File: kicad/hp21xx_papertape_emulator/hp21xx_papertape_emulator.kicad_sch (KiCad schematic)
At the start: 154 parts, among them J1 SWD, J2 SERIAL, J3 Micro_SD_Card_Det_Hirose_DM3AT, J5 Conn_02x13_Odd_Even, Q1 2N7002, Q10 2N7002, Q11 2N7002, Q12 BSS84, Q13 2N7002, Q14 2N7002, Q15 BSS84, Q2 2N7002, Q3 2N7002, Q4 2N7002, Q5 2N7002, Q6 2N7002, Q7 2N7002, Q8 2N7002, Q9 2N7002, SW1 Select, SW2 Up, SW3 Down, U1 TLV75533PDRV, U2 STM32F103C8Tx, U3 USBLC6-2SC6, U4 AP3012, U6 74LVC14, U7 74LVC245, Y1 8MHz

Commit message: Fixed issues.
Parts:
- removed R84, R90: 100, Resistor_SMD:R_0402_1005Metric, symbol Device:R_Small
- added C12, C13: 4.7u, Capacitor_SMD:C_1206_3216Metric, symbol Device:C_Small
- added R47, R48: 100, Resistor_SMD:R_0402_1005Metric, symbol Device:R_Small
- J5: now left out of the parts list
- Q1, Q10, Q11, Q13, Q14, Q2, Q3, Q4, Q5, Q6, Q7, Q8, Q9: value 2N7002 -> BSS138; LCSC C22446827 -> C53113928
- Q12, Q15: value BSS84 -> PMOS; LCSC C82079 -> (none)
- R104, R45, R56, R59, R62, R65, R68, R71, R74, R77, R80, R83: LCSC C25531 -> C25744
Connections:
- net GND: now also C12.2, C13.2
- net PU12V: now also C12.1
- net PU5V: now also C13.1
- net at Q15.2 (G): now also R48.2
- net at Q12.2 (G): now also R47.2
- net at Q14.1 (D), R89.2: now also R48.1
- net at Q13.1 (D), R85.2, R88.1: now also R47.1

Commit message: Fixed problems with net unconnected.
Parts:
- added R49, R50: 10k, Resistor_SMD:R_0402_1005Metric, symbol Device:R_Small
- Q12, Q15: value PMOS -> BSS84; LCSC (none) -> C41354933
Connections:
- net +12V: now also R50.1
- net +5V: now also R49.1
- net at Q15.2 (G), R48.2: now also R49.2
- net at Q12.2 (G), R47.2: now also R50.2

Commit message: spin 2
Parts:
- added D10, D11, D12, D13, D14, D15, D16, D17, D18, D19, D20, D21, D22, D23, D24, D25, D26, D27, D28, D29, D8, D9: BAT54J, Diode_SMD:D_SOD-523, symbol Diode:BAT54J
- added R51, R52: 10k, Resistor_SMD:R_0402_1005Metric, symbol Device:R_Small
- H2, H4, H6, H8: footprint MountingHole:MountingHole_2.2mm_M2 -> MountingHole:MountingHole_2.5mm
- L1: footprint Inductor_SMD:L_0805_2012Metric -> Inductor_SMD:L_Sunlord_SWPA3010S; LCSC C88172 -> C2049730
- Q1, Q10, Q11, Q13, Q14, Q2, Q3, Q4, Q5, Q6, Q7, Q8, Q9: symbol Simulation_SPICE:NMOS -> Transistor_FET:Q_NMOS_GSD
- Q12, Q15: symbol Simulation_SPICE:PMOS -> Transistor_FET:Q_PMOS_GSD
- R1, R2: value 2k -> 10k; LCSC C4109 -> C25744
- R11, R13, R15, R17, R24, R27, R33, R35, R37, R41: footprint Resistor_SMD:R_0402_1005Metric -> Resistor_SMD:R_0805_2012Metric; LCSC C25104 -> C17630
- R87: value 100k -> 1k; LCSC C25741 -> C11702
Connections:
- net +12V: now also Q12.2 (S); no longer Q12.1 (D)
- net +5V: now also Q15.2 (S); no longer Q15.1 (D)
- net GND: now also J3.9 (DET_B), Q1.2 (S), Q10.2 (S), Q11.2 (S), Q13.2 (S), Q14.2 (S), Q2.2 (S), Q3.2 (S), Q4.2 (S), Q5.2 (S), Q6.2 (S), Q7.2 (S), Q8.2 (S), Q9.2 (S), R51.2, R52.2; no longer Q1.3 (S), Q10.3 (S), Q11.3 (S), Q13.3 (S), Q14.3 (S), Q2.3 (S), Q3.3 (S), Q4.3 (S), Q5.3 (S), Q6.3 (S), Q7.3 (S), Q8.3 (S), Q9.3 (S)
- net OUT0: now also Q2.3 (D); no longer Q2.1 (D)
- net OUT1: now also Q3.3 (D); no longer Q3.1 (D)
- net OUT2: now also Q6.3 (D); no longer Q6.1 (D)
- net OUT3: now also Q7.3 (D); no longer Q7.1 (D)
- net OUT4: now also Q8.3 (D); no longer Q8.1 (D)
- net OUT5: now also Q9.3 (D); no longer Q9.1 (D)
- net OUT6: now also Q10.3 (D); no longer Q10.1 (D)
- net OUT7: now also Q11.3 (D); no longer Q11.1 (D)
- net OUTFP: now also Q1.3 (D); no longer Q1.1 (D)
- net OUTFR: now also Q4.3 (D); no longer Q4.1 (D)
- net PAPER_LOW: now also Q5.3 (D); no longer Q5.1 (D)
- net PU12V: now also D11.2 (A), D13.2 (A), D15.2 (A), D17.2 (A), D18.2 (A), D21.2 (A), D23.2 (A), D25.2 (A), D26.2 (A), D28.2 (A), D9.2 (A), R52.1; no longer R45.1, R56.1, R59.1, R62.1, R65.1, R68.1, R71.1, R74.1, R77.1, R80.1, R83.1
- net PU5V: now also D10.2 (A), D12.2 (A), D14.2 (A), D16.2 (A), D19.2 (A), D20.2 (A), D22.2 (A), D24.2 (A), D27.2 (A), D29.2 (A), D8.2 (A), R51.1; no longer R100.1, R101.1, R102.1, R103.1, R46.1, R94.1, R95.1, R96.1, R97.1, R98.1, R99.1
- net at R72.2, R73.1: now also Q8.1 (G); no longer Q8.2 (G)
- net at R48.1, R89.2: now also Q14.3 (D); no longer Q14.1 (D)
- net at R48.2, R49.2: now also Q15.1 (G); no longer Q15.2 (G)
- net at R10.2, R19.1: now also Q7.1 (G); no longer Q7.2 (G)
- net at R78.2, R79.1: now also Q10.1 (G); no longer Q10.2 (G)
- net at R86.2, R87.1: now also Q13.1 (G); no longer Q13.2 (G)
- net at R47.1, R85.2, R88.1: now also Q13.3 (D); no longer Q13.1 (D)
- net at R47.2, R50.2: now also Q12.1 (G); no longer Q12.2 (G)
- net at R63.2, R64.1: now also Q4.1 (G); no longer Q4.2 (G)
- net at R88.2, R93.1: now also Q14.1 (G); no longer Q14.2 (G)
- net at R75.2, R76.1: now also Q9.1 (G); no longer Q9.2 (G)
- net at R66.2, R67.1: now also Q5.1 (G); no longer Q5.2 (G)
- net at R81.2, R82.1: now also Q11.1 (G); no longer Q11.2 (G)
- net at R60.2, R61.1: now also Q3.1 (G); no longer Q3.2 (G)
- net at R69.2, R70.1: now also Q6.1 (G); no longer Q6.2 (G)
- net at R54.2, R55.1: now also Q1.1 (G); no longer Q1.2 (G)
- net at R57.2, R58.1: now also Q2.1 (G); no longer Q2.2 (G)
- new net: D18.1 (K), R56.1
- new net: D21.1 (K), R80.1
- new net: D17.1 (K), R62.1
- new net: D19.1 (K), R95.1
- new net: D13.1 (K), R65.1
- new net: D28.1 (K), R71.1
- new net: D15.1 (K), R68.1
- new net: D25.1 (K), R74.1
- new net: D10.1 (K), R100.1
- new net: D12.1 (K), R96.1
- new net: D8.1 (K), R94.1
- new net: D11.1 (K), R77.1
- new net: D22.1 (K), R98.1
- new net: D26.1 (K), R45.1
- new net: D24.1 (K), R103.1
- new net: D29.1 (K), R101.1
- new net: D27.1 (K), R102.1
- new net: D16.1 (K), R46.1
- new net: D20.1 (K), R99.1
- new net: D9.1 (K), R59.1
- new net: D14.1 (K), R97.1
- new net: D23.1 (K), R83.1
- no-connect marks 11 -> 10
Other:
- moved on the sheet: C10, C11, C12, C13, C8, C9, D4, D5, D6, D7, J1, J3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

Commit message: Fixed new spin.
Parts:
- added D30, D31, D32, D33, D34, D35, D36, D37, D38, D39: BZX584B5V1, Diode_SMD:D_SOD-523, symbol Diode:BZX384xxxx
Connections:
- net GND: now also D30.2 (A), D31.2 (A), D32.2 (A), D33.2 (A), D34.2 (A), D35.2 (A), D36.2 (A), D37.2 (A), D38.2 (A), D39.2 (A)
- net at R43.2, U6.1: now also D38.1 (K)
- net at R32.2, U7.9 (A7): now also D37.1 (K)
- net at R21.2, U7.4 (A2): now also D32.1 (K)
- net at R44.2, U6.3: now also D39.1 (K)
- net at R20.2, U7.2 (A0): now also D30.1 (K)
- net at R23.2, U7.8 (A6): now also D36.1 (K)
- net at R29.2, U7.3 (A1): now also D31.1 (K)
- net at R30.2, U7.5 (A3): now also D33.1 (K)
- net at R22.2, U7.6 (A4): now also D34.1 (K)
- net at R31.2, U7.7 (A5): now also D35.1 (K)
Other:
- moved on the sheet: R20, R21, R22, R23, R29, R30, R31, R32, R43, R44, U6A, U6B

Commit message: Fixed missing LCSC number for BAT54
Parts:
- D10, D11, D12, D13, D14, D15, D16, D17, D18, D19, D20, D21, D22, D23, D24, D25, D26, D27, D28, D29, D8, D9: LCSC (none) -> C51315114
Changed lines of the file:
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@@
 			)
 		)
+		(property "LCSC" "C51315114"
+			(at 341.63 110.49 90)
+			(effects
+				(font
+					(size 1.27 1.27)
+				)
+				(hide yes)
+			)
+		)
 		(pin "1"
 		)
@@
 			)
 		)
+		(property "LCSC" "C51315114"
+			(at 392.43 124.46 90)
+			(effects
+				(font
+					(size 1.27 1.27)
+				)
+				(hide yes)
+			)
+		)
 		(pin "1"
 		)
@@
 			)
 		)
+		(property "LCSC" "C51315114"
+			(at 334.01 110.49 90)
+			(effects
+				(font
+					(size 1.27 1.27)
+				)
+				(hide yes)
+			)
+		)
 		(pin "1"
 		)
@@
 			)
 		)
+		(property "LCSC" "C51315114"
+			(at 321.31 209.55 90)
+			(effects
+				(font
+					(size 1.27 1.27)
+				)
+				(hide yes)
+			)
+		)
 		(pin "1"
 		)
@@
 			)
 		)
+		(property "LCSC" "C51315114"
+			(at 368.3 205.74 90)
+			(effects
+				(font
+					(size 1.27 1.27)
+				)
+				(hide yes)
+			)
+		)
 		(pin "1"
 		)
@@
 			)
 		)
+		(property "LCSC" "C51315114"
+			(at 312.42 30.48 90)
+			(effects
+				(font
+					(size 1.27 1.27)
+				)
+				(hide yes)
+			)
+		)
 		(pin "1"
 		)
@@
 			)
 		)
+		(property "LCSC" "C51315114"
+			(at 383.54 30.48 90)
+			(effects
+				(font
+					(size 1.27 1.27)
+				)
+				(hide yes)
+			)
+		)
 		(pin "1"
 		)
@@
 			)
 		)
+		(property "LCSC" "C51315114"
+			(at 312.42 209.55 90)
+			(effects
+				(font
+					(size 1.27 1.27)
+				)
+				(hide yes)
+			)
+		)
 		(pin "1"
 		)
@@
 			)
 		)
+		(property "LCSC" "C51315114"
+			(at 250.19 115.57 90)
+			(effects
+				(font
+					(size 1.27 1.27)
+				)
+				(hide yes)
+			)
+		)
 		(pin "1"
 		)
@@
 			)
 		)
+		(property "LCSC" "C51315114"
+			(at 289.56 116.84 90)
+			(effects
+				(font
+					(size 1.27 1.27)
+				)
+				(hide yes)
+			)
+		)
 		(pin "1"
 		)
@@
 			)
 		)
+		(property "LCSC" "C51315114"
+			(at 381 82.55 90)
+			(effects
+				(font
+					(size 1.27 1.27)
+				)
+				(hide yes)
+			)
+		)
 		(pin "1"
 		)
@@
 			)
 		)
+		(property "LCSC" "C51315114"
+			(at 309.88 74.93 90)
+			(effects
+				(font
+					(size 1.27 1.27)
+				)
+				(hide yes)
+			)
+		)
 		(pin "1"
 		)
@@
 			)
 		)
+		(property "LCSC" "C51315114"
+			(at 281.94 116.84 90)
+			(effects
+				(font
+					(size 1.27 1.27)
+				)
+				(hide yes)
+			)
+		)
 		(pin "1"
 		)
@@
 			)
 		)
+		(property "LCSC" "C51315114"
+			(at 259.08 115.57 90)
+			(effects
+				(font
+					(size 1.27 1.27)
+				)
+				(hide yes)
+			)
+		)
 		(pin "1"
 		)
@@
 			)
 		)
+		(property "LCSC" "C51315114"
+			(at 384.81 124.46 90)
+			(effects
+				(font
+					(size 1.27 1.27)
+				)
+				(hide yes)
+			)
+		)
 		(pin "1"
 		)
@@
 			)
 		)
+		(property "LCSC" "C51315114"
+			(at 346.71 30.48 90)
+			(effects
+				(font
+					(size 1.27 1.27)
+				)
+				(hide yes)
+			)
+		)
 		(pin "1"
 		)
@@
 			)
 		)
+		(property "LCSC" "C51315114"
+			(at 360.68 205.74 90)
+			(effects
+				(font
+					(size 1.27 1.27)
+				)
+				(hide yes)
+			)
+		)
 		(pin "1"
 		)
@@
 			)
 		)
+		(property "LCSC" "C51315114"
+			(at 339.09 30.48 90)
+			(effects
+				(font
+					(size 1.27 1.27)
+				)
+				(hide yes)
+			)
+		)
 		(pin "1"
 		)
@@
 			)
 		)
+		(property "LCSC" "C51315114"
+			(at 300.99 74.93 90)
+			(effects
+				(font
+					(size 1.27 1.27)
+				)
+				(hide yes)
+			)
+		)
 		(pin "1"
 		)
@@
 			)
 		)
+		(property "LCSC" "C51315114"
+			(at 377.19 30.48 90)
+			(effects
+				(font
+					(size 1.27 1.27)
+				)
+				(hide yes)
+			)
+		)
 		(pin "1"
 		)
@@
 			)
 		)
+		(property "LCSC" "C51315114"
+			(at 306.07 30.48 90)
+			(effects
+				(font
+					(size 1.27 1.27)
+				)
+				(hide yes)
+			)
+		)
 		(pin "1"
 		)
@@
 			(effects
 				(font
+					(size 1.27 1.27)
+				)
+				(hide yes)
+			)
+		)
+		(property "LCSC" "C51315114"
+			(at 388.62 82.55 90)
+			(effects
+				(font

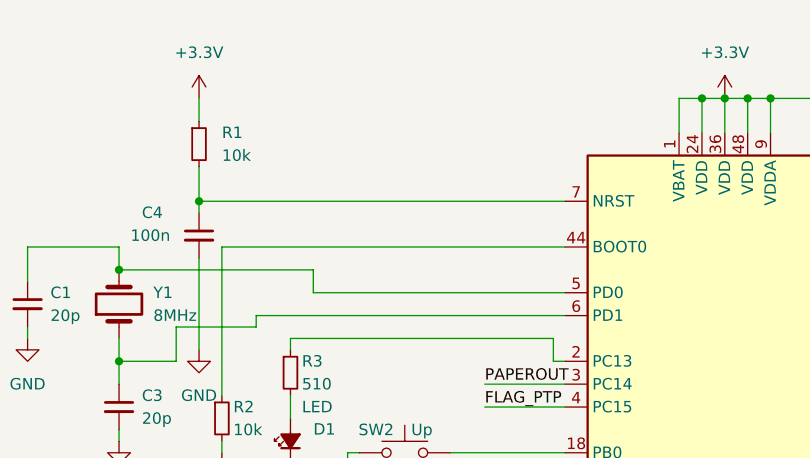
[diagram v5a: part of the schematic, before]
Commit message: Added jumper to be able to use serial bootstrap mode.
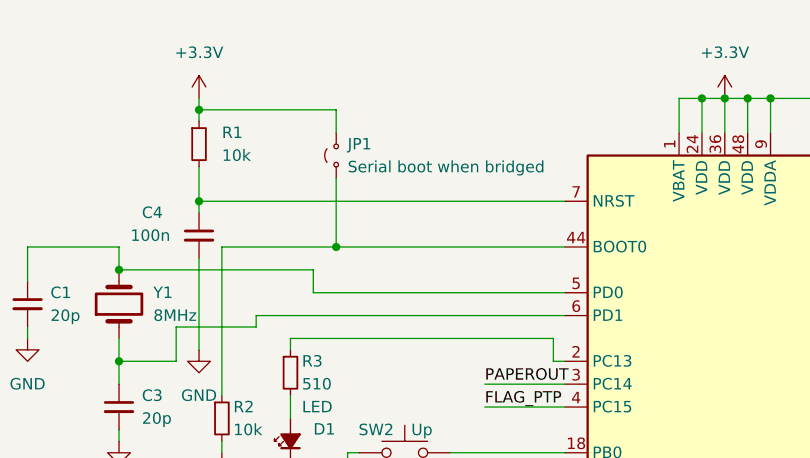
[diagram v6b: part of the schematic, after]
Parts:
- added JP1: Serial boot when bridged, Connector_PinHeader_2.54mm:PinHeader_1x02_P2.54mm_Vertical, symbol Jumper:Jumper_2_Small_Open
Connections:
- net +3.3V: now also JP1.2 (B)
- net at R2.1, U2.44 (BOOT0): now also JP1.1 (A)
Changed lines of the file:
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@@
 	)
 	(junction
+		(at 34.29 20.32)
+		(diameter 0)
+		(color 0 0 0 0)
+	)
+	(junction
 		(at 383.54 41.91)
 		(diameter 0)
@@
 	)
 	(junction
+		(at 49.53 35.56)
+		(diameter 0)
+		(color 0 0 0 0)
+	)
+	(junction
 		(at 199.39 62.23)
 		(diameter 0)
@@
 	(wire
 		(pts
-			(xy 34.29 19.05) (xy 34.29 21.59)
+			(xy 34.29 19.05) (xy 34.29 20.32)
 		)
 		(stroke
@@
 	(wire
 		(pts
-			(xy 36.83 35.56) (xy 74.93 35.56)
+			(xy 36.83 35.56) (xy 49.53 35.56)
 		)
 		(stroke
@@
 	(wire
 		(pts
+			(xy 34.29 20.32) (xy 34.29 21.59)
+		)
+		(stroke
+			(width 0)
+			(type default)
+		)
+	)
+	(wire
+		(pts
 			(xy 209.55 17.78) (xy 203.2 17.78)
 		)
@@
 	(wire
 		(pts
+			(xy 49.53 27.94) (xy 49.53 35.56)
+		)
+		(stroke
+			(width 0)
+			(type default)
+		)
+	)
+	(wire
+		(pts
 			(xy 243.84 17.78) (xy 250.19 17.78)
 		)
@@
 	(wire
 		(pts
+			(xy 49.53 20.32) (xy 49.53 22.86)
+		)
+		(stroke
+			(width 0)
+			(type default)
+		)
+	)
+	(wire
+		(pts
 			(xy 53.34 99.06) (xy 57.15 99.06)
 		)
@@
 	(wire
 		(pts
+			(xy 34.29 20.32) (xy 49.53 20.32)
+		)
+		(stroke
+			(width 0)
+			(type default)
+		)
+	)
+	(wire
+		(pts
 			(xy 119.38 250.19) (xy 121.92 250.19)
 		)
@@
 	(wire
 		(pts
+			(xy 49.53 35.56) (xy 74.93 35.56)
+		)
+		(stroke
+			(width 0)
+			(type default)
+		)
+	)
+	(wire
+		(pts
 			(xy 260.35 186.69) (xy 260.35 180.34)
 		)
@@
 					(unit 1)
 				)
+			)
+		)
+	)
+	(symbol
+		(lib_id "Jumper:Jumper_2_Small_Open")
+		(at 49.53 25.4 90)
+		(unit 1)
+		(exclude_from_sim no)
+		(in_bom yes)
+		(on_board yes)
+		(dnp no)
+		(fields_autoplaced yes)
+		(property "Reference" "JP1"
+			(at 50.8 24.1299 90)
+			(effects
+				(font
+					(size 1.27 1.27)
+				)
+				(justify right)
+			)
+		)
+		(property "Value" "Serial boot when bridged"
+			(at 50.8 26.6699 90)
+			(effects
+				(font
+					(size 1.27 1.27)
+				)
+				(justify right)
+			)
+		)
+		(property "Footprint" "Connector_PinHeader_2.54mm:PinHeader_1x02_P2.54mm_Vertical"
+			(at 49.53 25.4 0)
+			(effects
+				(font
+					(size 1.27 1.27)
+				)
+				(hide yes)
+			)
+		)
+		(property "Datasheet" "~"
+			(at 49.53 25.4 0)
+			(effects
+				(font
+					(size 1.27 1.27)
+				)
+				(hide yes)
+			)
+		)
+		(property "Description" "Jumper, 2-pole, small symbol, open"
+			(at 49.53 25.4 0)
+			(effects
+				(font
+					(size 1.27 1.27)
+				)
+				(hide yes)
+			)
+		)
+		(pin "2"
+		)
+		(pin "1"
+		)
+		(instances
+			(project ""
+				(path "/dca39f23-b951-4c9b-9ea5-0122ff9447f1"
+					(reference "JP1")
+					(unit 1)
+				)
